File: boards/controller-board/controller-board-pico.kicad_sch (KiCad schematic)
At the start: 49 parts, among them J1 Phoenix 1935161, J2 Conn_01x02, J3 Conn_01x02, J4 Conn_01x02, J5 Conn_01x03, J6 Phoenix 1995499, Q1 PMV45EN, Q2 Goford_G11S_20V_11A, U2 ADS1015IRUGR, U4 RPi_Pico, U5 MCP4728

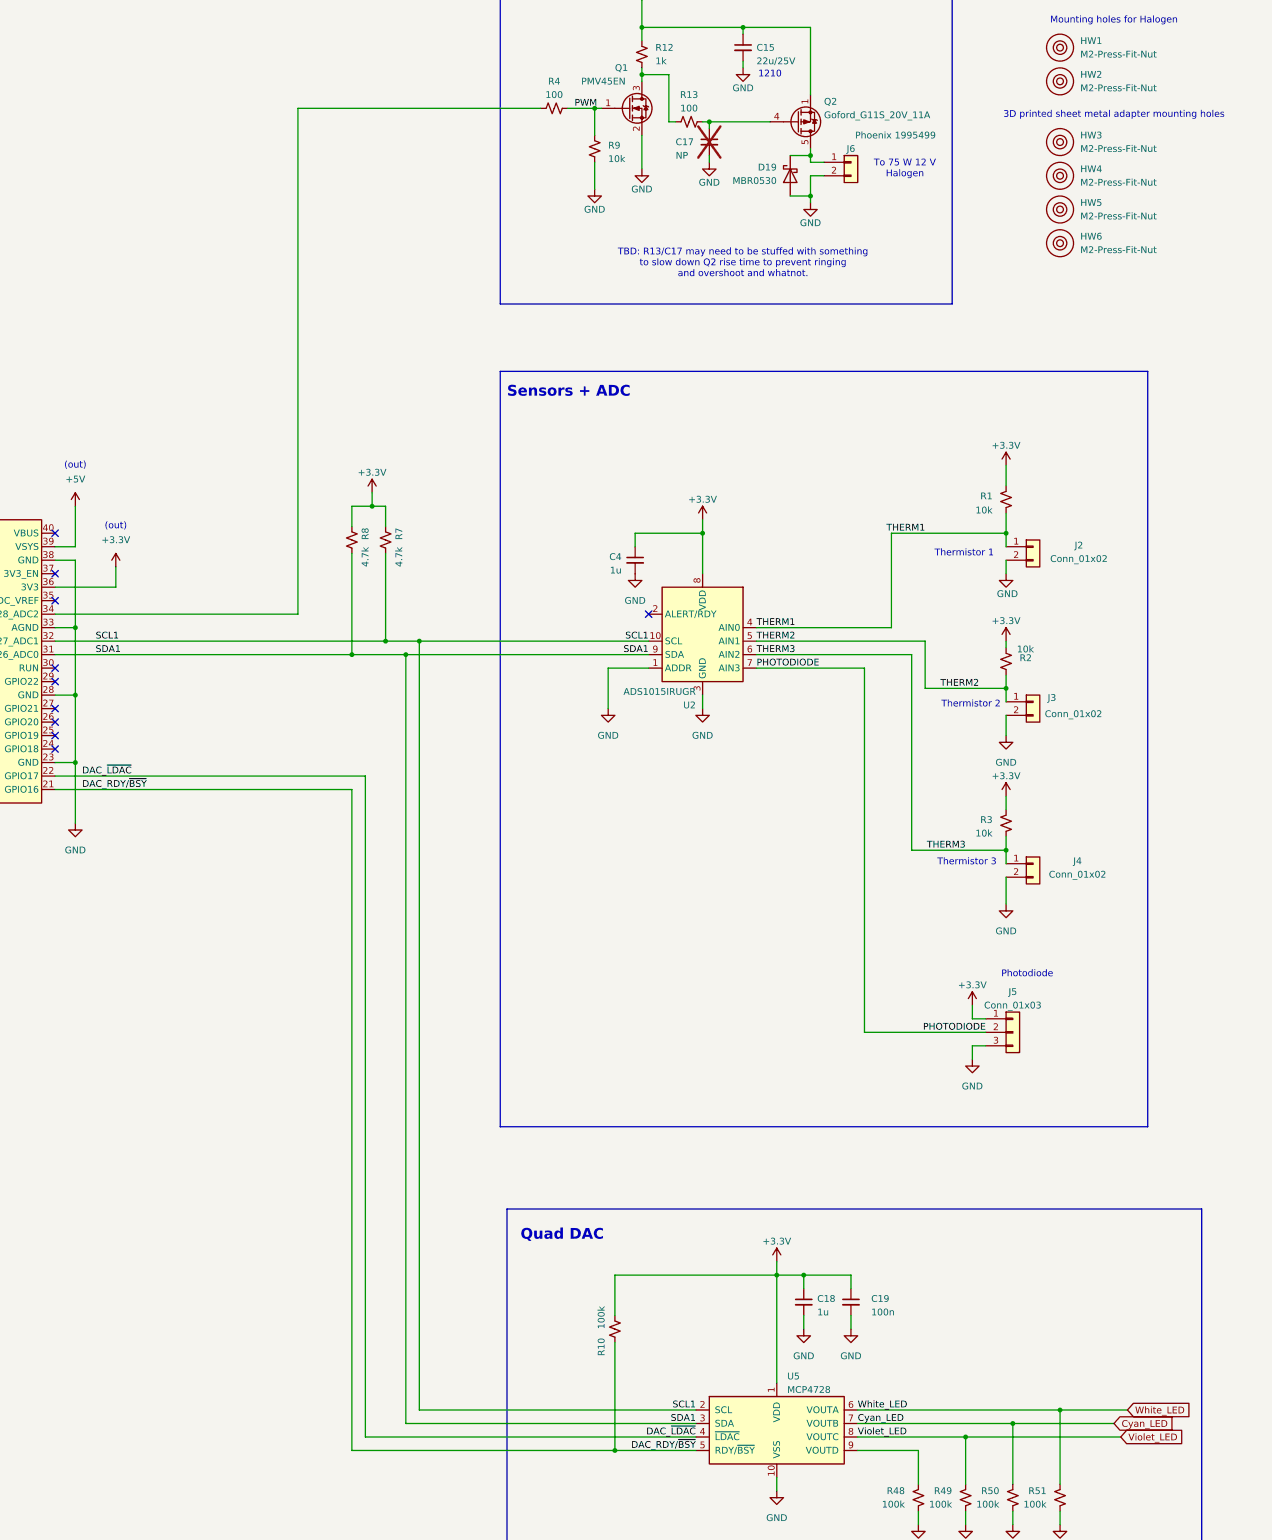
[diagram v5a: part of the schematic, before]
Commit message: Layout complete; no airwires. Still needs polishing.
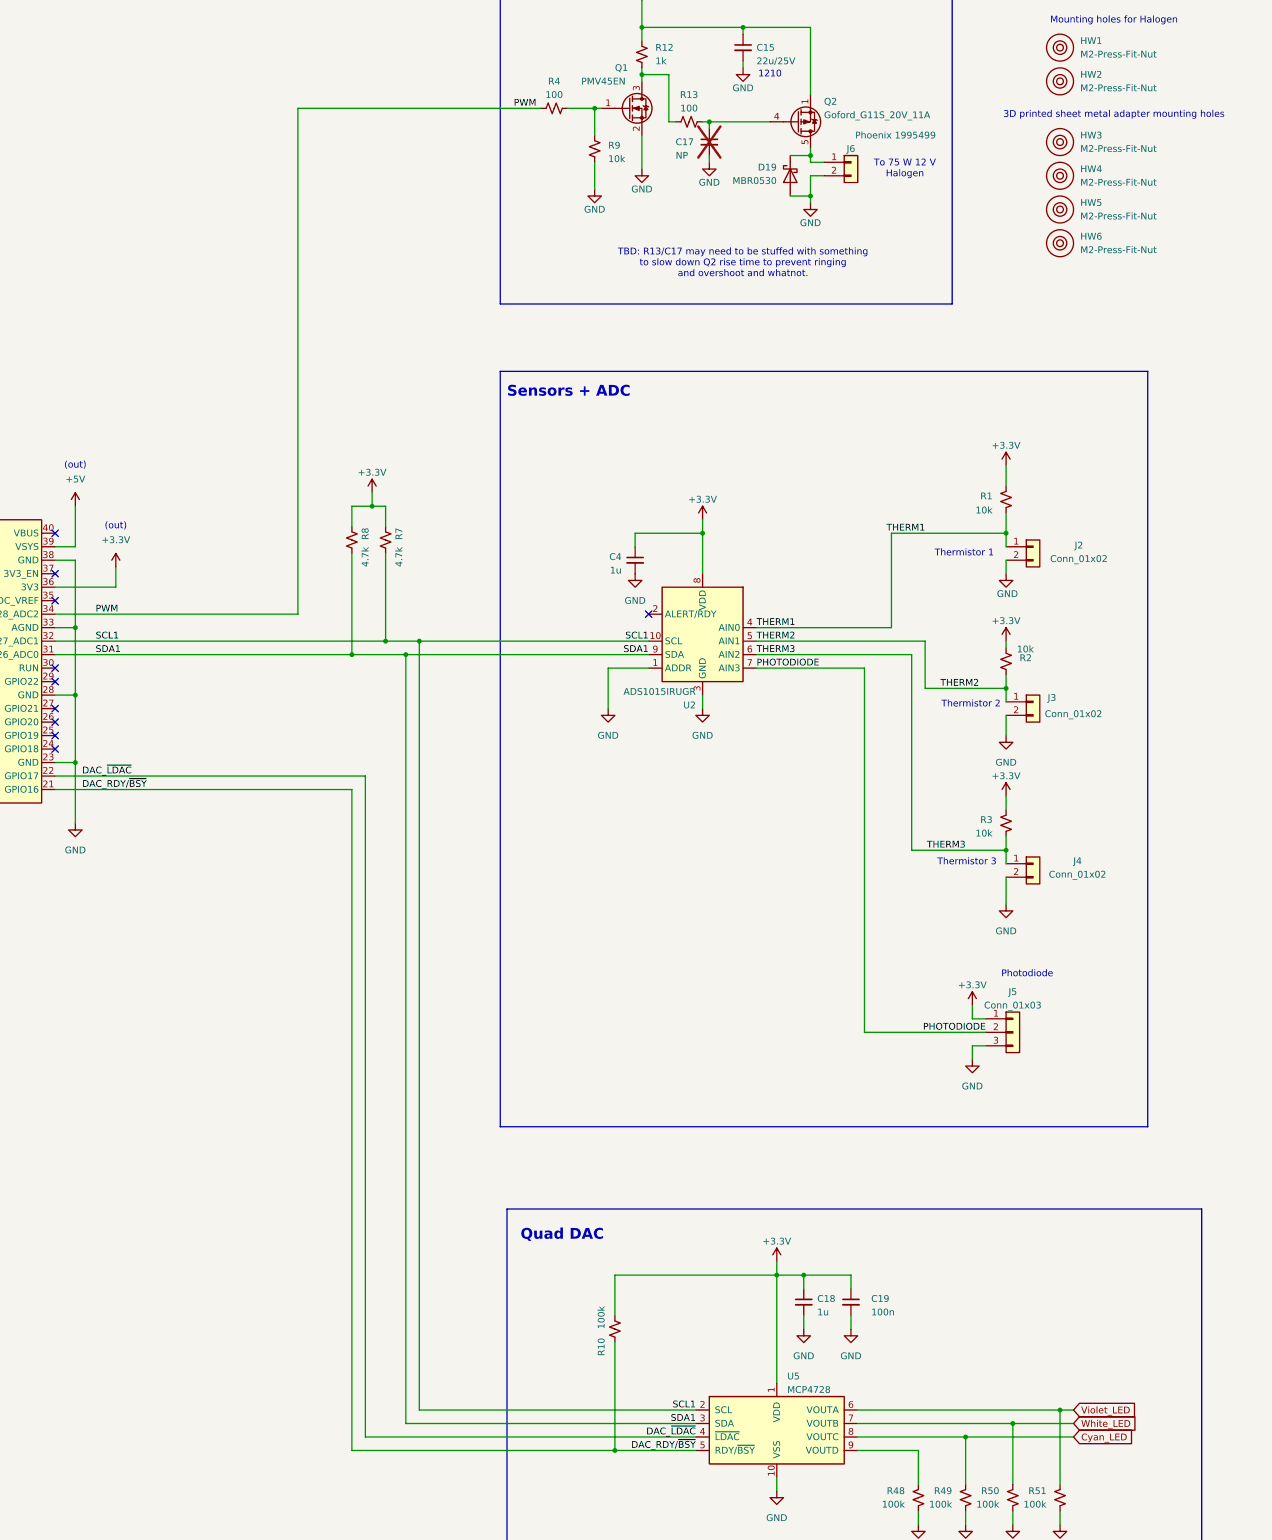
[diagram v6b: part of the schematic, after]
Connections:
- net Cyan_LED: now also R49.1, U5.8 (VOUTC); no longer R50.1, U5.7 (VOUTB)
- net PWM: now also R4.1, U4.34 (GPIO28_ADC2); no longer Q1.1 (G), R4.2, R9.1
- net Violet_LED: now also R51.1, U5.6 (VOUTA); no longer R49.1, U5.8 (VOUTC)
- net White_LED: now also R50.1, U5.7 (VOUTB); no longer R51.1, U5.6 (VOUTA)
- new net: Q1.1 (G), R4.2, R9.1
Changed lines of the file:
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@@
+	)
+	(junction
+		(at 316.23 64.77)
+		(diameter 0)
+		(color 0 0 0 0)
+	)
+	(junction
+		(at 341.63 299.72)
+		(diameter 0)
+		(color 0 0 0 0)
+	)
+	(junction
+		(at 384.81 189.23)
+		(diameter 0)
+		(color 0 0 0 0)
+	)
+	(junction
+		(at 153.67 190.5)
+		(diameter 0)
+		(color 0 0 0 0)
+	)
+	(junction
+		(at 316.23 73.66)
+		(diameter 0)
+		(color 0 0 0 0)
+	)
+	(junction
+		(at 327.66 160.02)
+		(diameter 0)
+		(color 0 0 0 0)
+	)
+	(junction
+		(at 377.19 330.2)
+		(diameter 0)
+		(color 0 0 0 0)
+	)
+	(junction
+		(at 307.34 80.01)
+		(diameter 0)
+		(color 0 0 0 0)
+	)
+	(junction
+		(at 346.71 299.72)
+		(diameter 0)
+		(color 0 0 0 0)
+	)
+	(junction
+		(at 271.78 182.88)
+		(diameter 0)
+		(color 0 0 0 0)
+	)
+	(junction
+		(at 274.32 180.34)
+		(diameter 0)
+		(color 0 0 0 0)
+	)
+	(junction
+		(at 384.81 219.71)
+		(diameter 0)
+		(color 0 0 0 0)
+	)
+	(junction
+		(at 101.6 71.12)
+		(diameter 0)
+		(color 0 0 0 0)
+	)
+	(junction
+		(at 311.15 332.74)
+		(diameter 0)
+		(color 0 0 0 0)
+	)
+	(junction
+		(at 209.55 203.2)
+		(diameter 0)
+		(color 0 0 0 0)
+	)
+	(junction
+		(at 265.43 154.94)
+		(diameter 0)
+		(color 0 0 0 0)
+	)
+	(junction
+		(at 384.81 160.02)
+		(diameter 0)
+		(color 0 0 0 0)
+	)
+	(junction
+		(at 261.62 182.88)
+		(diameter 0)
+		(color 0 0 0 0)
+	)
+	(junction
+		(at 209.55 190.5)
+		(diameter 0)
+		(color 0 0 0 0)
+	)
+	(junction
+		(at 347.98 88.9)
+		(diameter 0)
+		(color 0 0 0 0)
+	)
+	(junction
+		(at 101.6 68.58)
+		(diameter 0)
+		(color 0 0 0 0)
+	)
+	(junction
+		(at 153.67 203.2)
+		(diameter 0)
+		(color 0 0 0 0)
 	)
 	(junction
@@
 	)
 	(junction
-		(at 316.23 64.77)
-		(diameter 0)
-		(color 0 0 0 0)
-	)
-	(junction
-		(at 341.63 299.72)
-		(diameter 0)
-		(color 0 0 0 0)
-	)
-	(junction
-		(at 384.81 189.23)
-		(diameter 0)
-		(color 0 0 0 0)
-	)
-	(junction
-		(at 153.67 190.5)
-		(diameter 0)
-		(color 0 0 0 0)
-	)
-	(junction
-		(at 316.23 73.66)
-		(diameter 0)
-		(color 0 0 0 0)
-	)
-	(junction
-		(at 327.66 160.02)
-		(diameter 0)
-		(color 0 0 0 0)
-	)
-	(junction
-		(at 307.34 80.01)
-		(diameter 0)
-		(color 0 0 0 0)
-	)
-	(junction
-		(at 346.71 299.72)
-		(diameter 0)
-		(color 0 0 0 0)
-	)
-	(junction
-		(at 271.78 182.88)
-		(diameter 0)
-		(color 0 0 0 0)
-	)
-	(junction
-		(at 274.32 180.34)
-		(diameter 0)
-		(color 0 0 0 0)
-	)
-	(junction
-		(at 384.81 219.71)
-		(diameter 0)
-		(color 0 0 0 0)
-	)
-	(junction
-		(at 101.6 71.12)
-		(diameter 0)
-		(color 0 0 0 0)
-	)
-	(junction
-		(at 311.15 332.74)
-		(diameter 0)
-		(color 0 0 0 0)
-	)
-	(junction
-		(at 209.55 203.2)
-		(diameter 0)
-		(color 0 0 0 0)
-	)
-	(junction
-		(at 265.43 154.94)
-		(diameter 0)
-		(color 0 0 0 0)
-	)
-	(junction
-		(at 384.81 160.02)
-		(diameter 0)
-		(color 0 0 0 0)
-	)
-	(junction
-		(at 261.62 182.88)
-		(diameter 0)
-		(color 0 0 0 0)
-	)
-	(junction
-		(at 209.55 190.5)
-		(diameter 0)
-		(color 0 0 0 0)
-	)
-	(junction
-		(at 347.98 88.9)
-		(diameter 0)
-		(color 0 0 0 0)
-	)
-	(junction
-		(at 101.6 68.58)
-		(diameter 0)
-		(color 0 0 0 0)
-	)
-	(junction
-		(at 153.67 203.2)
-		(diameter 0)
-		(color 0 0 0 0)
-	)
-	(junction
-		(at 377.19 330.2)
-		(diameter 0)
-		(color 0 0 0 0)
-	)
-	(junction
 		(at 386.08 327.66)
 		(diameter 0)
@@
 	(wire
 		(pts
+			(xy 394.97 325.12) (xy 397.51 325.12)
+		)
+		(stroke
+			(width 0)
+			(type default)
+		)
+	)
+	(wire
+		(pts
 			(xy 205.74 162.56) (xy 209.55 162.56)
 		)
@@
 	(wire
 		(pts
+			(xy 377.19 330.2) (xy 397.51 330.2)
+		)
+		(stroke
+			(width 0)
+			(type default)
+		)
+	)
+	(wire
+		(pts
 			(xy 187.96 213.36) (xy 187.96 214.63)
 		)
@@
 	(wire
 		(pts
-			(xy 377.19 330.2) (xy 406.4 330.2)
-		)
-		(stroke
-			(width 0)
-			(type default)
-		)
-	)
-	(wire
-		(pts
 			(xy 367.03 182.88) (xy 367.03 219.71)
 		)
@@
 	(wire
 		(pts
+			(xy 386.08 327.66) (xy 397.51 327.66)
+		)
+		(stroke
+			(width 0)
+			(type default)
+		)
+	)
+	(wire
+		(pts
 			(xy 307.34 80.01) (xy 307.34 85.09)
 		)
@@
 	(wire
 		(pts
-			(xy 386.08 327.66) (xy 405.13 327.66)
-		)
-		(stroke
-			(width 0)
-			(type default)
-		)
-	)
-	(wire
-		(pts
 			(xy 384.81 189.23) (xy 384.81 191.77)
 		)
@@
 		(pts
 			(xy 158.75 170.18) (xy 170.18 170.18)
-		)
-		(stroke
-			(width 0)
-			(type default)
-		)
-	)
-	(wire
-		(pts
-			(xy 394.97 325.12) (xy 407.67 325.12)
 		)
 		(stroke
@@
 		)
 	)
-	(label "White_LED"
-		(at 356.87 325.12 0)
-		(effects
-			(font
-				(size 1.27 1.27)
-			)
-			(justify left bottom)
-		)
-	)
 	(label "DAC_~{LDAC}"
 		(at 326.39 330.2 180)
@@
 		)
 	)
+	(label "PWM"
+		(at 213.36 175.26 0)
+		(effects
+			(font
+				(size 1.27 1.27)
+			)
+			(justify left bottom)
+		)
+	)
 	(label "THERM1"
 		(at 369.57 160.02 180)
@@
 		)
 	)
-	(label "PWM"
-		(at 303.53 80.01 0)
-		(effects
-			(font
-				(size 1.27 1.27)
-			)
-			(justify left bottom)
-		)
-	)
 	(label "SDA1"
 		(at 326.39 327.66 180)
@@
 		)
 	)
-	(label "Cyan_LED"
-		(at 356.87 327.66 0)
-		(effects
-			(font
-				(size 1.27 1.27)
-			)
-			(justify left bottom)
-		)
-	)
 	(label "SDA1"
 		(at 317.5 182.88 180)
@@
 		)
 	)
-	(label "Violet_LED"
-		(at 356.87 330.2 0)
-		(effects
-			(font
-				(size 1.27 1.27)
-			)
-			(justify left bottom)
-		)
-	)
 	(label "THERM1"
 		(at 337.82 177.8 0)
@@
 		)
 	)
+	(label "PWM"
+		(at 292.1 80.01 0)
+		(effects
+			(font
+				(size 1.27 1.27)
+			)
+			(justify left bottom)
+		)
+	)
 	(label "DAC_~{LDAC}"
 		(at 210.82 205.74 0)
@@
 	(global_label "Cyan_LED"
 		(shape input)
-		(at 405.13 327.66 0)
+		(at 397.51 330.2 0)
 		(fields_autoplaced yes)
 		(effects
@@
 		)
 		(property "Intersheetrefs" "${INTERSHEET_REFS}"
-			(at 417.0655 327.66 0)
+			(at 409.4455 330.2 0)
 			(effects
 				(font
@@
 	(global_label "Violet_LED"
 		(shape input)
-		(at 406.4 330.2 0)
+		(at 397.51 325.12 0)
 		(fields_autoplaced yes)
 		(effects
@@
 		)
 		(property "Intersheetrefs" "${INTERSHEET_REFS}"
-			(at 419.1218 330.2 0)
+			(at 410.2318 325.12 0)
 			(effects
 				(font
@@
 	(global_label "White_LED"
 		(shape input)
-		(at 407.67 325.12 0)
+		(at 397.51 327.66 0)
 		(fields_autoplaced yes)
 		(effects
@@
 		)
 		(property "Intersheetrefs" "${INTERSHEET_REFS}"
-			(at 420.0894 325.12 0)
+			(at 409.9294 327.66 0)
 			(effects
 				(font

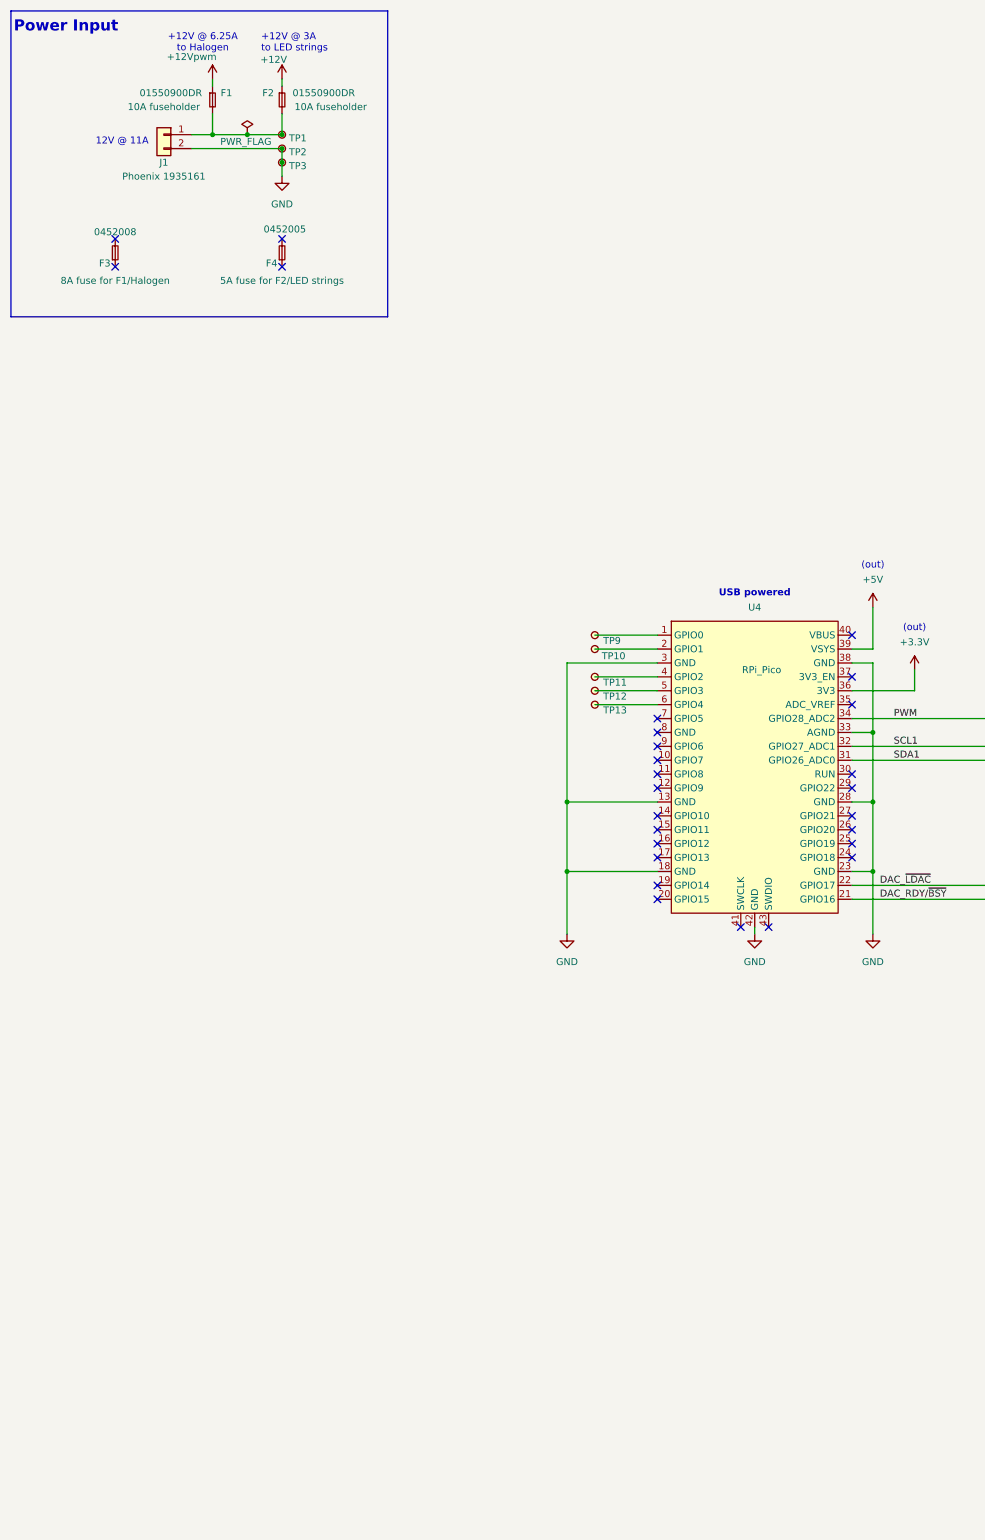
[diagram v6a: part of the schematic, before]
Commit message: Update to KiCAD 9; fix library issue in oresat-ics, update ERC exclusions
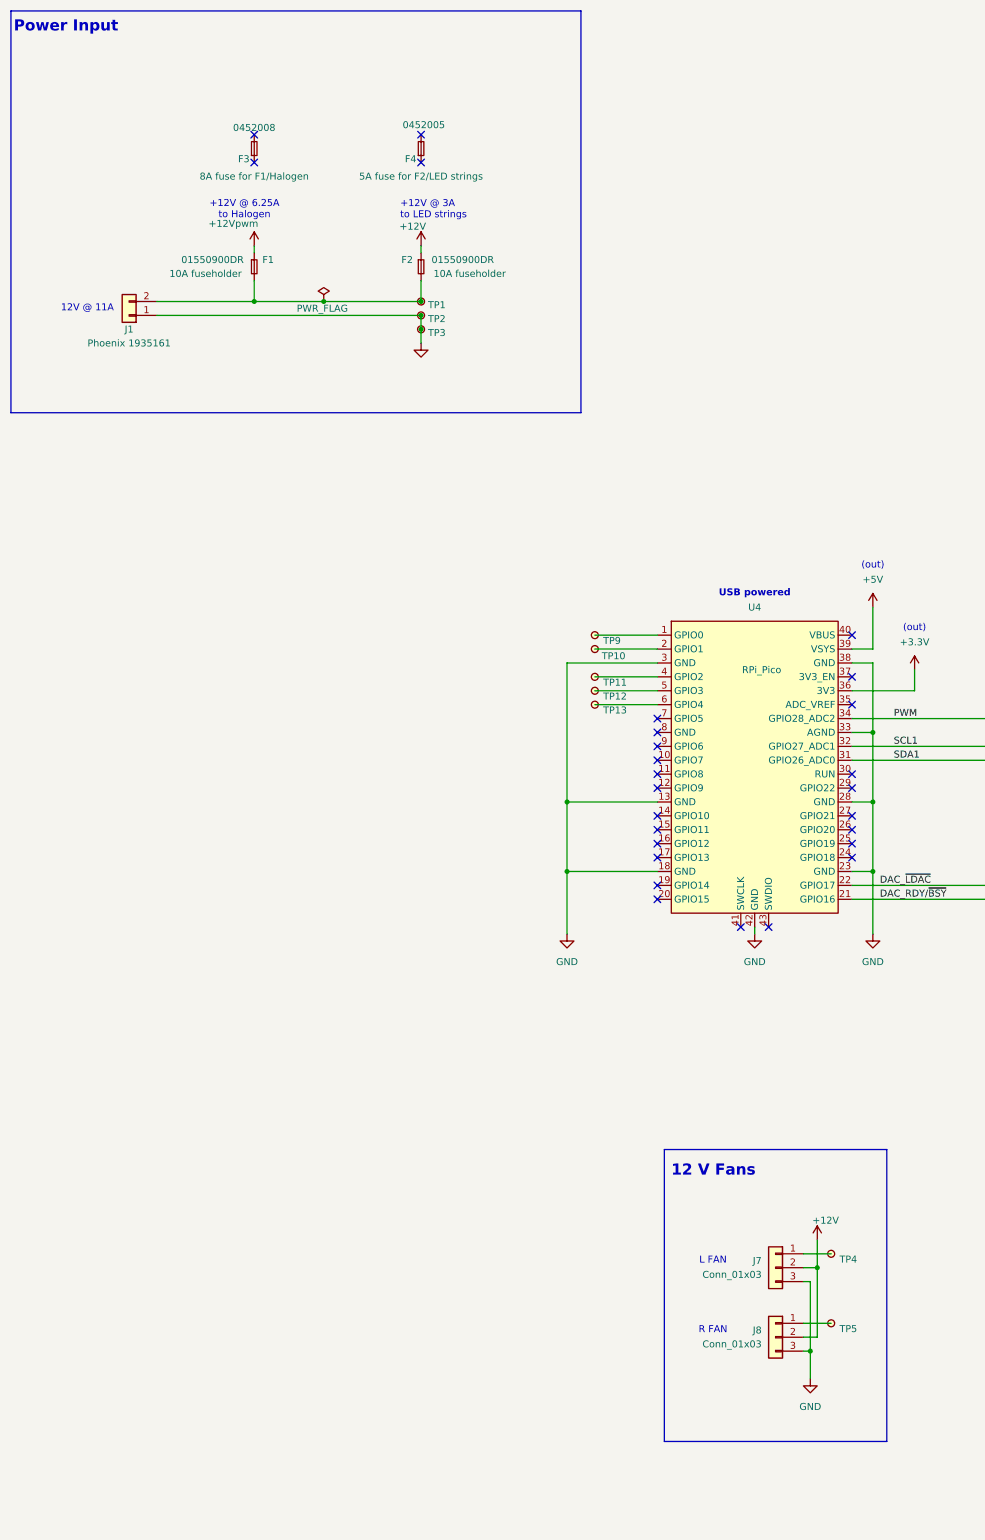
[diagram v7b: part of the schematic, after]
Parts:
- added J7, J8: Conn_01x03, Connector_PinHeader_2.54mm:PinHeader_1x03_P2.54mm_Vertical, symbol Connector_Generic:Conn_01x03
- added TP4, TP5: TestPoint-MinTH, oresat-misc:TestPoint-MinTH, symbol oresat-misc:TestPoint-MinTH
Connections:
- net +12V: now also J7.2 (Pin_2), J8.2 (Pin_2)
- net GND: now also J1.1 (Pin_1), J7.3 (Pin_3), J8.3 (Pin_3); no longer J1.2 (Pin_2)
- net at F1.2, F2.2, TP1.1: now also J1.2 (Pin_2); no longer J1.1 (Pin_1)
- new net: J7.1 (Pin_1), TP4.1
- new net: J8.1 (Pin_1), TP5.1
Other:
- note added: "12 V Fans"
- note added: "L FAN"
- note added: "R FAN"
- moved on the sheet: F1, F2, J1, TP1, TP2, TP3
